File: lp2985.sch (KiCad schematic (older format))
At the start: 6 parts, among them U3 LP2985LV

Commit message: added lots of stuff
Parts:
- D1, D2: footprint Diodes_SMD:SMA_Standard -> Diodes_SMD:SOD-323
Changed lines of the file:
@@
 EESchema Schematic File Version 2
+LIBS:stm32f4_lqfp64_mpu6050-rescue
 LIBS:power
 LIBS:device
@@
 LIBS:minimal
 LIBS:alis_parts
+LIBS:sensors
+LIBS:stm32
 LIBS:stm32f4_lqfp64_mpu6050-cache
 EELAYER 25 0
@@
 $Descr A4 11693 8268
 encoding utf-8
-Sheet 6 7
+Sheet 6 10
 Title ""
 Date ""
@@
 F 0 "D2" V 5096 2982 50  0000 R CNN
 F 1 "D_Schottky_Small" V 5004 2982 50  0000 R CNN
-F 2 "Diodes_SMD:SMA_Standard" V 5050 3050 50  0001 C CNN
+F 2 "Diodes_SMD:SOD-323" V 5050 3050 50  0001 C CNN
 F 3 "" V 5050 3050 50  0000 C CNN
 	1    5050 3050
@@
 F 0 "D1" V 4746 2982 50  0000 R CNN
 F 1 "D_Schottky_Small" V 4654 2982 50  0000 R CNN
-F 2 "Diodes_SMD:SMA_Standard" V 4700 3050 50  0001 C CNN
+F 2 "Diodes_SMD:SOD-323" V 4700 3050 50  0001 C CNN
 F 3 "" V 4700 3050 50  0000 C CNN
 	1    4700 3050
@@
 $EndComp
 $Comp
-L GND #PWR23
+L GND #PWR24
 U 1 1 569BA880
 P 6000 4350
-F 0 "#PWR23" H 6000 4100 50  0001 C CNN
+F 0 "#PWR24" H 6000 4100 50  0001 C CNN
 F 1 "GND" H 6008 4176 50  0000 C CNN
 F 2 "" H 6000 4350 50  0000 C CNN

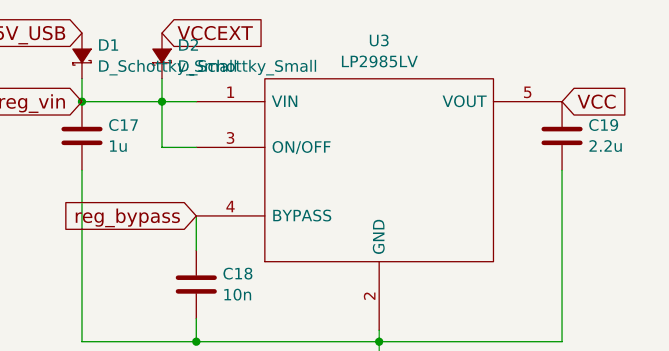
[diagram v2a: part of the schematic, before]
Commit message: changed some netnames
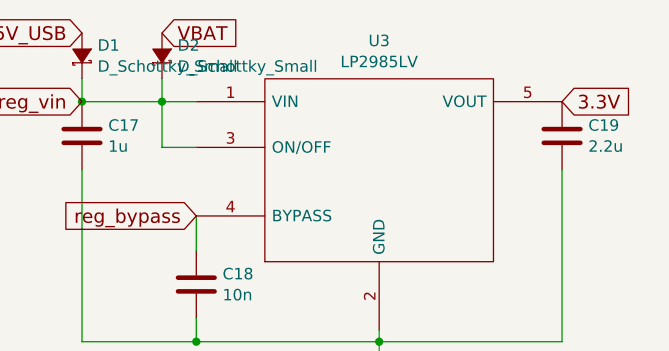
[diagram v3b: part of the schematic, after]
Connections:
- net VCC renamed 3.3V
- net VCCEXT renamed VBAT
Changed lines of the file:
@@
 $EndComp
 Text GLabel 6800 3250 2    60   Input ~ 0
-VCC
+3.3V
 Text GLabel 4700 2950 0    60   Input ~ 0
 +5V_USB
@@
 $EndComp
 Text GLabel 5050 2950 2    60   Input ~ 0
-VCCEXT
+VBAT
 $Comp
 L C C19
@@
 $EndComp
 $Comp
-L GND #PWR24
+L GND #PWR025
 U 1 1 569BA880
 P 6000 4350
-F 0 "#PWR24" H 6000 4100 50  0001 C CNN
+F 0 "#PWR025" H 6000 4100 50  0001 C CNN
 F 1 "GND" H 6008 4176 50  0000 C CNN
 F 2 "" H 6000 4350 50  0000 C CNN

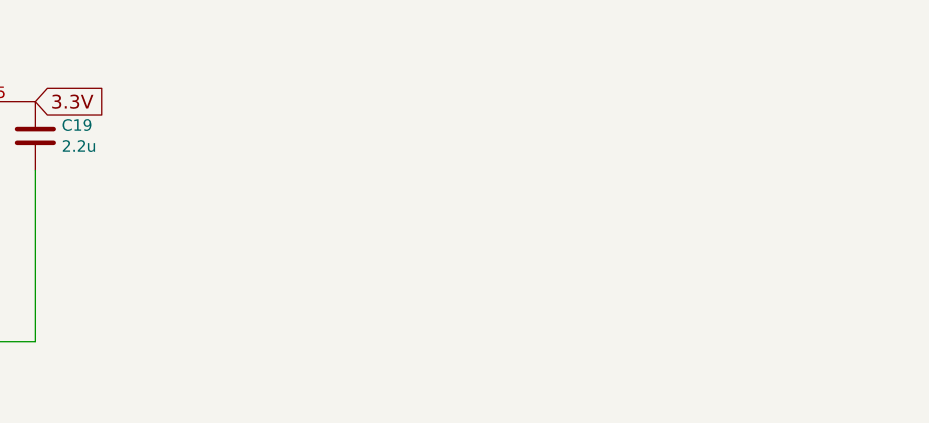
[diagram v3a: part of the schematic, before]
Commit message: OSD running on breadboard
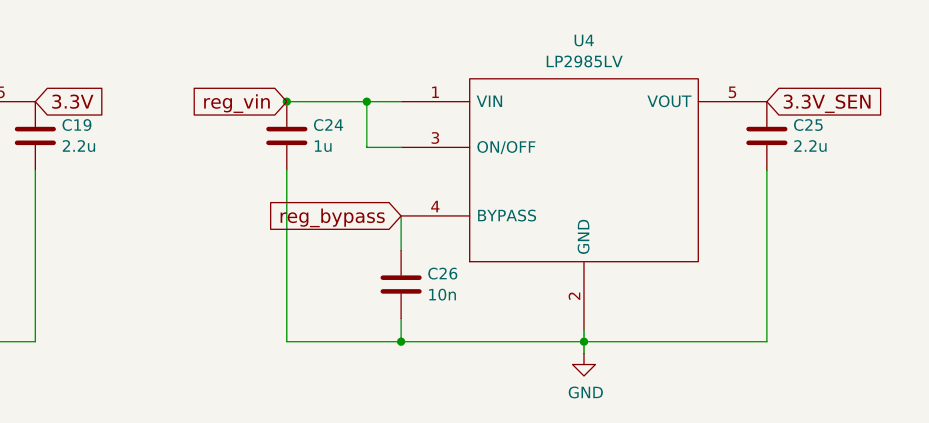
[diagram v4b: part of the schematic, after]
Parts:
- added C24: 1u, Capacitors_SMD:C_0402, symbol C
- added C25: 2.2u, Capacitors_SMD:C_0603, symbol C
- added C26: 10n, Capacitors_SMD:C_0402, symbol C
- added U4: LP2985LV, TO_SOT_Packages_SMD:SOT-23-5, symbol LP2985LV
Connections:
- net GND: now also C24.2, C25.2, C26.2, U4.2 (GND)
- net reg_bypass: now also C26.1, U4.4 (BYPASS)
- net reg_vin: now also C24.1, U4.1 (VIN), U4.3 (ON/OFF)
- new net 3.3V_SEN: C25.1, U4.5 (VOUT)
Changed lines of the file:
@@
 $EndComp
 $Comp
-L GND #PWR025
+L GND #PWR029
 U 1 1 569BA880
 P 6000 4350
-F 0 "#PWR025" H 6000 4100 50  0001 C CNN
+F 0 "#PWR029" H 6000 4100 50  0001 C CNN
 F 1 "GND" H 6008 4176 50  0000 C CNN
 F 2 "" H 6000 4350 50  0000 C CNN
@@
 	1    0    0    -1
 $EndComp
+Wire Wire Line
+	7900 3250 8400 3250
+Connection ~ 8250 3250
+Wire Wire Line
+	8250 3450 8400 3450
+Connection ~ 8400 4300
+Wire Wire Line
+	8400 4200 8400 4300
+Wire Wire Line
+	8400 3750 8400 3900
+Wire Wire Line
+	10000 4300 10000 3550
+Connection ~ 9200 4300
+Wire Wire Line
+	9200 4250 9200 4350
+Wire Wire Line
+	7900 4300 10000 4300
+Wire Wire Line
+	7900 3550 7900 4300
+Connection ~ 7900 3250
+Text GLabel 7900 3250 0    60   Input ~ 0
+reg_vin
+Text GLabel 8400 3750 0    60   Input ~ 0
+reg_bypass
+Text GLabel 10000 3250 2    60   Input ~ 0
+3.3V_SEN
+$Comp
+L C C26
+U 1 1 571EB9EE
+P 8400 4050
+F 0 "C26" H 8515 4096 50  0000 L CNN
+F 1 "10n" H 8515 4004 50  0000 L CNN
+F 2 "Capacitors_SMD:C_0402" H 8438 3900 50  0001 C CNN
+F 3 "" H 8400 4050 50  0000 C CNN
+	1    8400 4050
+	1    0    0    -1
+$EndComp
+$Comp
+L C C24
+U 1 1 571EB9F5
+P 7900 3400
+F 0 "C24" H 8015 3446 50  0000 L CNN
+F 1 "1u" H 8015 3354 50  0000 L CNN
+F 2 "Capacitors_SMD:C_0402" H 7938 3250 50  0001 C CNN
+F 3 "" H 7900 3400 50  0000 C CNN
+	1    7900 3400
+	1    0    0    -1
+$EndComp
+$Comp
+L C C25
+U 1 1 571EB9FC
+P 10000 3400
+F 0 "C25" H 10115 3446 50  0000 L CNN
+F 1 "2.2u" H 10115 3354 50  0000 L CNN
+F 2 "Capacitors_SMD:C_0603" H 10038 3250 50  0001 C CNN
+F 3 "" H 10000 3400 50  0000 C CNN
+	1    10000 3400
+	1    0    0    -1
+$EndComp
+$Comp
+L GND #PWR030
+U 1 1 571EBA03
+P 9200 4350
+F 0 "#PWR030" H 9200 4100 50  0001 C CNN
+F 1 "GND" H 9208 4176 50  0000 C CNN
+F 2 "" H 9200 4350 50  0000 C CNN
+F 3 "" H 9200 4350 50  0000 C CNN
+	1    9200 4350
+	1    0    0    -1
+$EndComp
+$Comp
+L LP2985LV U4
+U 1 1 571EBA09
+P 9200 3550
+F 0 "U4" H 9200 4116 50  0000 C CNN
+F 1 "LP2985LV" H 9200 4024 50  0000 C CNN
+F 2 "TO_SOT_Packages_SMD:SOT-23-5" H 9200 3550 50  0001 C CNN
+F 3 "" H 9200 3550 50  0000 C CNN
+	1    9200 3550
+	1    0    0    -1
+$EndComp
+Wire Wire Line
+	8250 3450 8250 3250
 $EndSCHEMATC

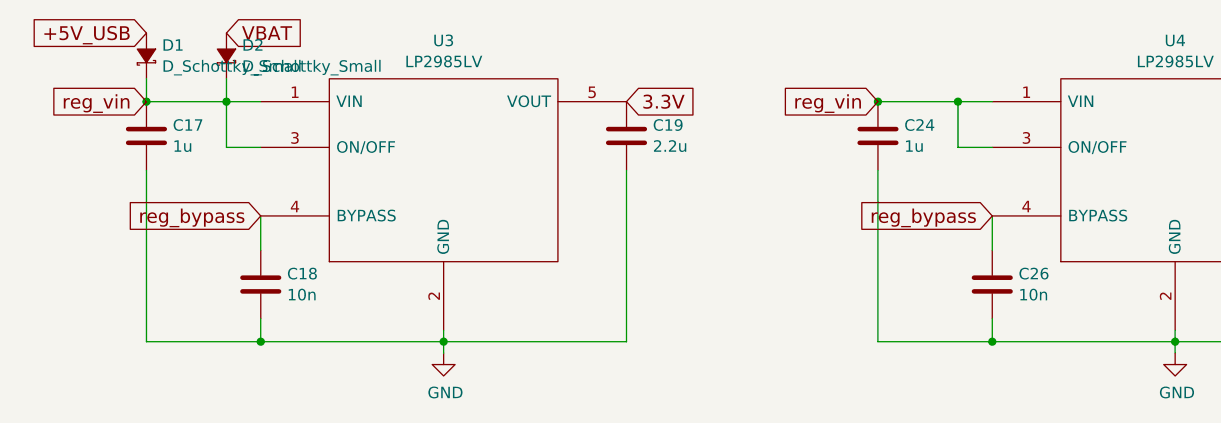
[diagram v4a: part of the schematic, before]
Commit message: power traces routed
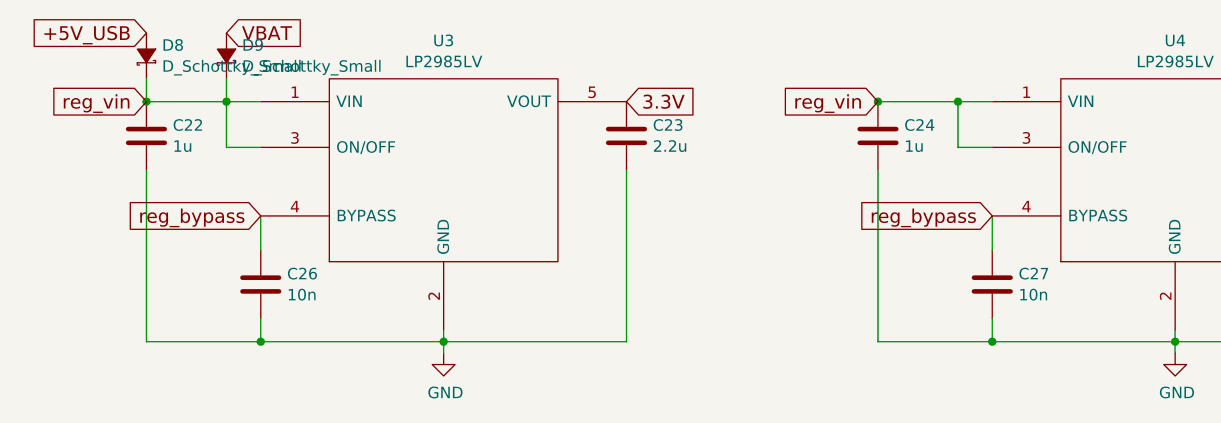
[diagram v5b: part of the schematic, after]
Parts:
- C22: renamed from C17; footprint Capacitors_SMD:C_0402 -> Capacitors_SMD:C_0603
- C24: footprint Capacitors_SMD:C_0402 -> Capacitors_SMD:C_0603
- C26: renamed from C18; footprint Capacitors_SMD:C_0402 -> Capacitors_SMD:C_0603
- C27: renamed from C26; footprint Capacitors_SMD:C_0402 -> Capacitors_SMD:C_0603
- renumbered C19 to C23, D1 to D8, D2 to D9
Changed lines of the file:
@@
 $Descr A4 11693 8268
 encoding utf-8
-Sheet 6 7
+Sheet 6 8
 Title ""
 Date ""
@@
 reg_bypass
 $Comp
-L D_Schottky_Small D2
+L D_Schottky_Small D9
 U 1 1 569BA85A
 P 5050 3050
-F 0 "D2" V 5096 2982 50  0000 R CNN
+F 0 "D9" V 5096 2982 50  0000 R CNN
 F 1 "D_Schottky_Small" V 5004 2982 50  0000 R CNN
 F 2 "Diodes_SMD:SOD-323" V 5050 3050 50  0001 C CNN
@@
 $EndComp
 $Comp
-L D_Schottky_Small D1
+L D_Schottky_Small D8
 U 1 1 569BA861
 P 4700 3050
-F 0 "D1" V 4746 2982 50  0000 R CNN
+F 0 "D8" V 4746 2982 50  0000 R CNN
 F 1 "D_Schottky_Small" V 4654 2982 50  0000 R CNN
 F 2 "Diodes_SMD:SOD-323" V 4700 3050 50  0001 C CNN
@@
 +5V_USB
 $Comp
-L C C18
+L C C26
 U 1 1 569BA86A
 P 5200 4050
-F 0 "C18" H 5315 4096 50  0000 L CNN
+F 0 "C26" H 5315 4096 50  0000 L CNN
 F 1 "10n" H 5315 4004 50  0000 L CNN
-F 2 "Capacitors_SMD:C_0402" H 5238 3900 50  0001 C CNN
+F 2 "Capacitors_SMD:C_0603" H 5238 3900 50  0001 C CNN
 F 3 "" H 5200 4050 50  0000 C CNN
 	1    5200 4050
@@
 $EndComp
 $Comp
-L C C17
+L C C22
 U 1 1 569BA871
 P 4700 3400
-F 0 "C17" H 4815 3446 50  0000 L CNN
+F 0 "C22" H 4815 3446 50  0000 L CNN
 F 1 "1u" H 4815 3354 50  0000 L CNN
-F 2 "Capacitors_SMD:C_0402" H 4738 3250 50  0001 C CNN
+F 2 "Capacitors_SMD:C_0603" H 4738 3250 50  0001 C CNN
 F 3 "" H 4700 3400 50  0000 C CNN
 	1    4700 3400
@@
 VBAT
 $Comp
-L C C19
+L C C23
 U 1 1 569BA879
 P 6800 3400
-F 0 "C19" H 6915 3446 50  0000 L CNN
+F 0 "C23" H 6915 3446 50  0000 L CNN
 F 1 "2.2u" H 6915 3354 50  0000 L CNN
 F 2 "Capacitors_SMD:C_0603" H 6838 3250 50  0001 C CNN
@@
 $EndComp
 $Comp
-L GND #PWR029
+L GND #PWR019
 U 1 1 569BA880
 P 6000 4350
-F 0 "#PWR029" H 6000 4100 50  0001 C CNN
+F 0 "#PWR019" H 6000 4100 50  0001 C CNN
 F 1 "GND" H 6008 4176 50  0000 C CNN
 F 2 "" H 6000 4350 50  0000 C CNN
@@
 3.3V_SEN
 $Comp
-L C C26
+L C C27
 U 1 1 571EB9EE
 P 8400 4050
-F 0 "C26" H 8515 4096 50  0000 L CNN
+F 0 "C27" H 8515 4096 50  0000 L CNN
 F 1 "10n" H 8515 4004 50  0000 L CNN
-F 2 "Capacitors_SMD:C_0402" H 8438 3900 50  0001 C CNN
+F 2 "Capacitors_SMD:C_0603" H 8438 3900 50  0001 C CNN
 F 3 "" H 8400 4050 50  0000 C CNN
 	1    8400 4050
@@
 F 0 "C24" H 8015 3446 50  0000 L CNN
 F 1 "1u" H 8015 3354 50  0000 L CNN
-F 2 "Capacitors_SMD:C_0402" H 7938 3250 50  0001 C CNN
+F 2 "Capacitors_SMD:C_0603" H 7938 3250 50  0001 C CNN
 F 3 "" H 7900 3400 50  0000 C CNN
 	1    7900 3400
@@
 $EndComp
 $Comp
-L GND #PWR030
+L GND #PWR020
 U 1 1 571EBA03
 P 9200 4350
-F 0 "#PWR030" H 9200 4100 50  0001 C CNN
+F 0 "#PWR020" H 9200 4100 50  0001 C CNN
 F 1 "GND" H 9208 4176 50  0000 C CNN
 F 2 "" H 9200 4350 50  0000 C CNN

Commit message: routing done except for ground, but ugly
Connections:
- net reg_bypass: no longer names the net of C26.1, U3.4 (BYPASS)
- net reg_bypass: no longer C27.1, U4.4 (BYPASS)
- new net: C27.1, U4.4 (BYPASS)
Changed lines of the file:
@@
 Text GLabel 4700 3250 0    60   Input ~ 0
 reg_vin
-Text GLabel 5200 3750 0    60   Input ~ 0
-reg_bypass
 $Comp
 L D_Schottky_Small D9
@@
 Text GLabel 7900 3250 0    60   Input ~ 0
 reg_vin
-Text GLabel 8400 3750 0    60   Input ~ 0
-reg_bypass
 Text GLabel 10000 3250 2    60   Input ~ 0
 3.3V_SEN

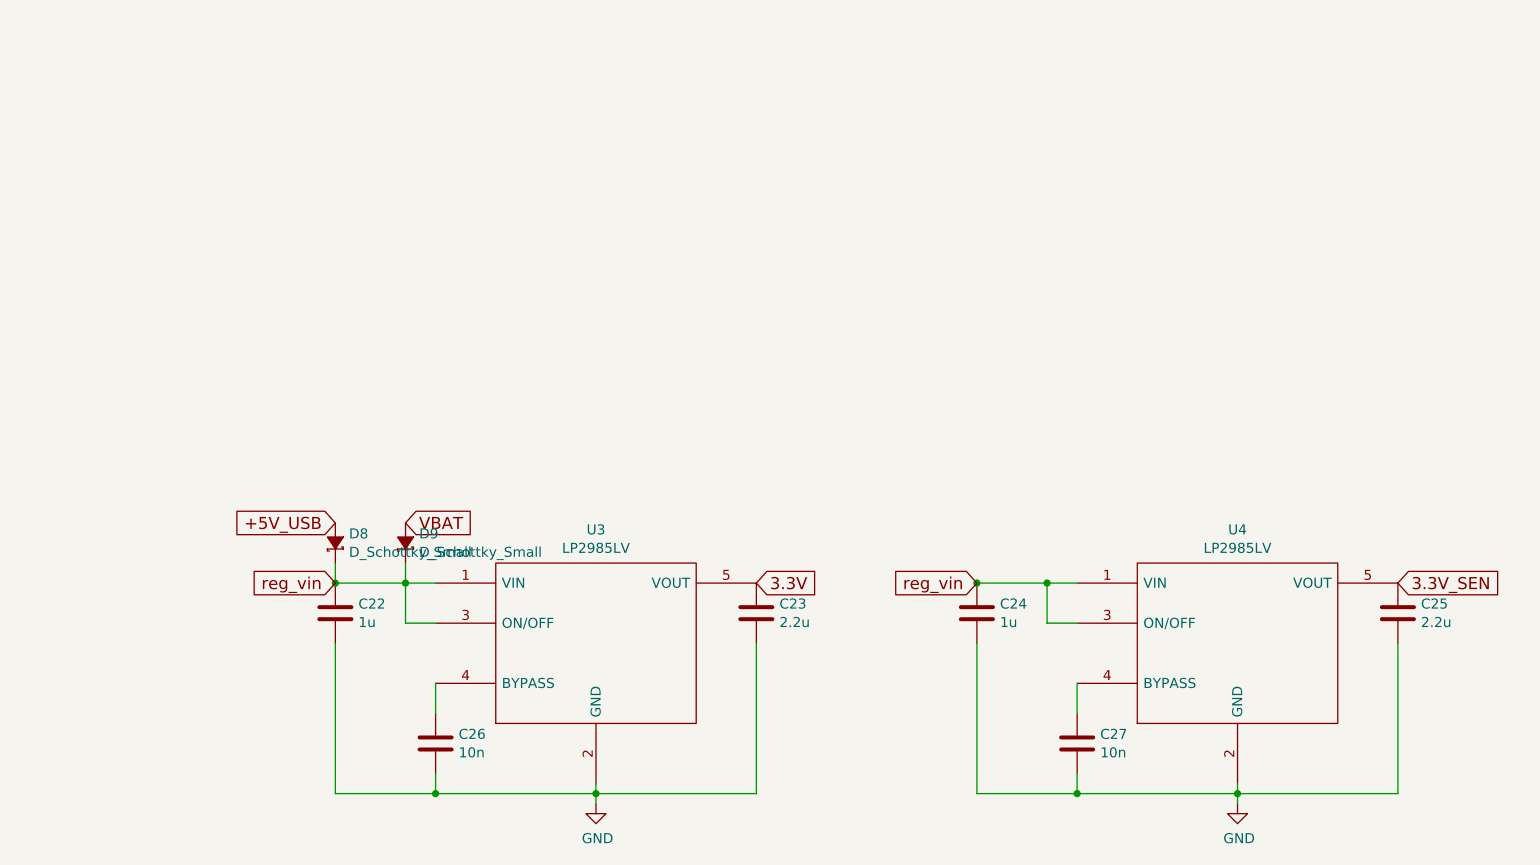
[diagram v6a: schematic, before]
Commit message: routing finished - essential signals only
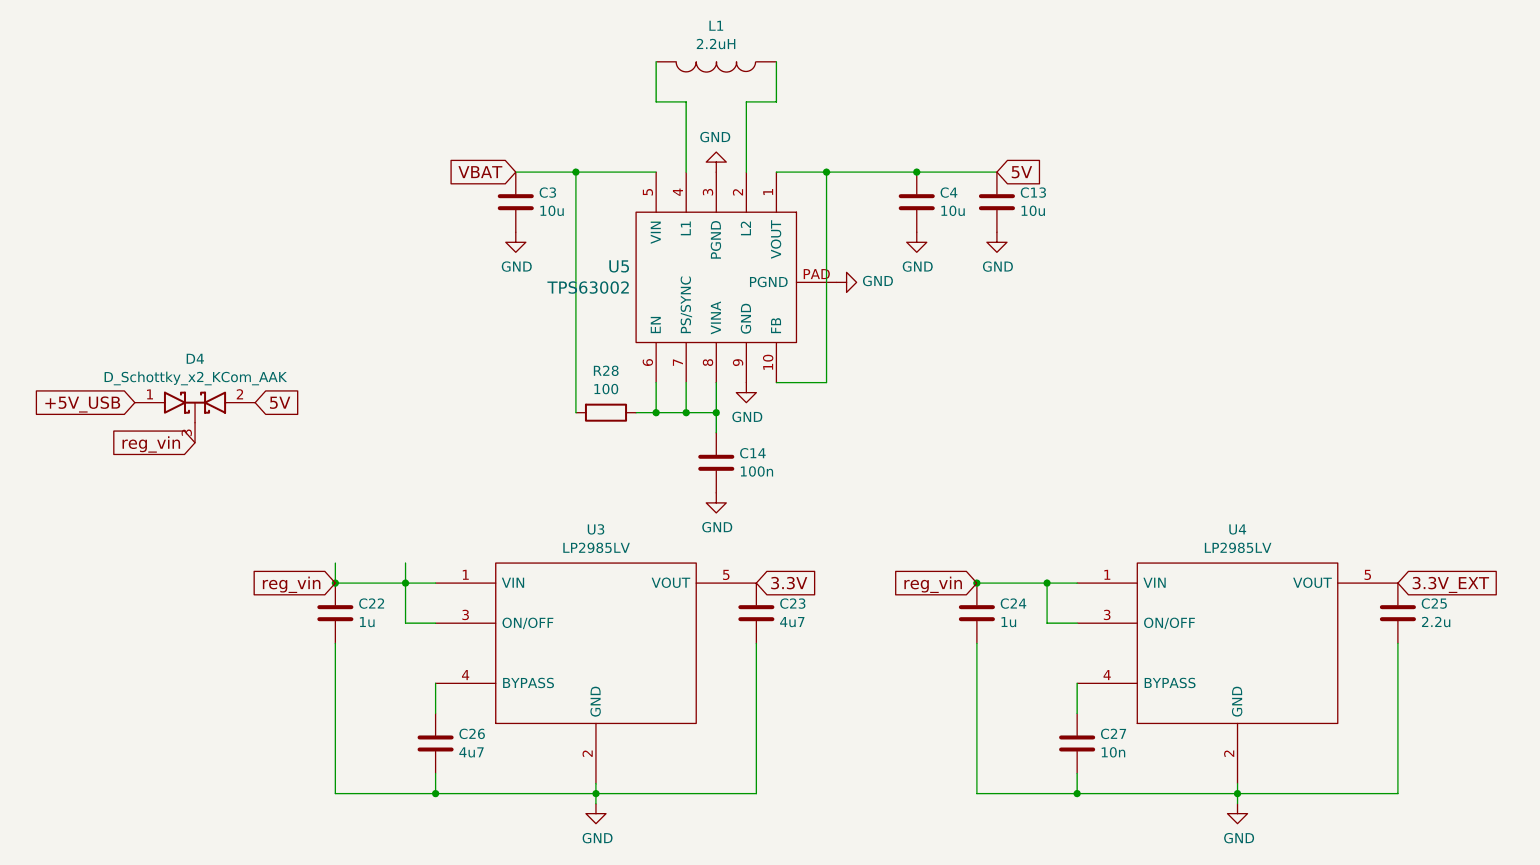
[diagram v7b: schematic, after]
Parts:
- removed D8, D9: D_Schottky_Small, Diodes_SMD:SOD-323, symbol D_Schottky_Small
- added C13, C3, C4: 10u, Capacitors_SMD:C_0603, symbol C
- added C14: 100n, Capacitors_SMD:C_0402, symbol C
- added D4: D_Schottky_x2_KCom_AAK, TO_SOT_Packages_SMD:SOT-23, symbol D_Schottky_x2_KCom_AAK
- added L1: 2.2uH, alis_parts:Choke_SMD_Taiyo_NR3015, symbol INDUCTOR
- added R28: 100, Resistors_SMD:R_0402, symbol R
- added U5: TPS63002, alis_parts:TPS63002, symbol TPS63002
- C22, C24, C27: footprint Capacitors_SMD:C_0603 -> Capacitors_SMD:C_0402
- C23: value 2.2u -> 4u7
- C26: value 10n -> 4u7
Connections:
- net labels added: 3.3V_EXT, 5V
- net labels removed: 3.3V_SEN
- wire segments 19 -> 34
